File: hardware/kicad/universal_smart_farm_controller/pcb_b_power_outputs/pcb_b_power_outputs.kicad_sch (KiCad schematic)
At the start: 55 parts, among them J1 Conn_01x12, J10 Conn_01x02, J11 Conn_01x02, J12 Conn_01x02, J13 Conn_01x02, J14 Conn_01x02, J15 Conn_01x02, J16 Conn_01x02, J17 Conn_01x02, J18 Conn_01x02, Q1 AO3400A, Q2 AO3400A, Q3 AO3400A, Q4 AO3400A, Q5 AO3400A, Q6 AO3400A, Q7 AO3400A, Q8 AO3400A

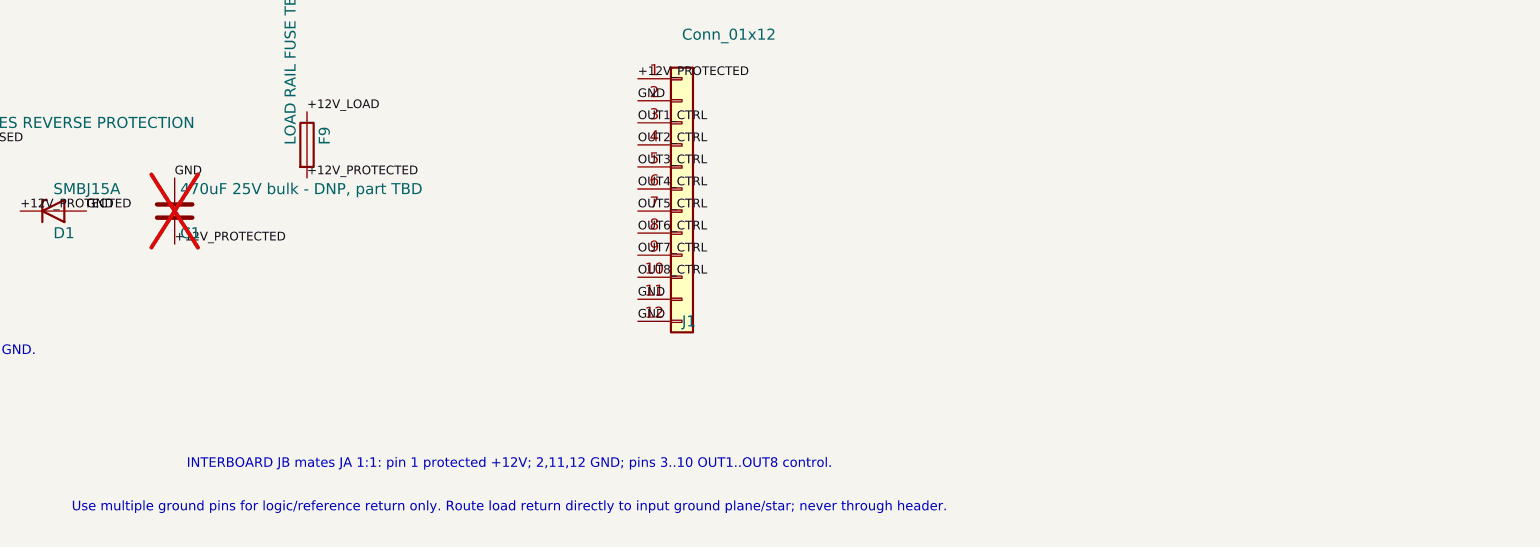
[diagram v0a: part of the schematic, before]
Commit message: Add PCB-B power LED, document PCB-A GPIO2 status LED, fix ADS1X15 lib_deps name
Co-authored-by: tomnyle <175001228+tomnyle@users.noreply.github.com>
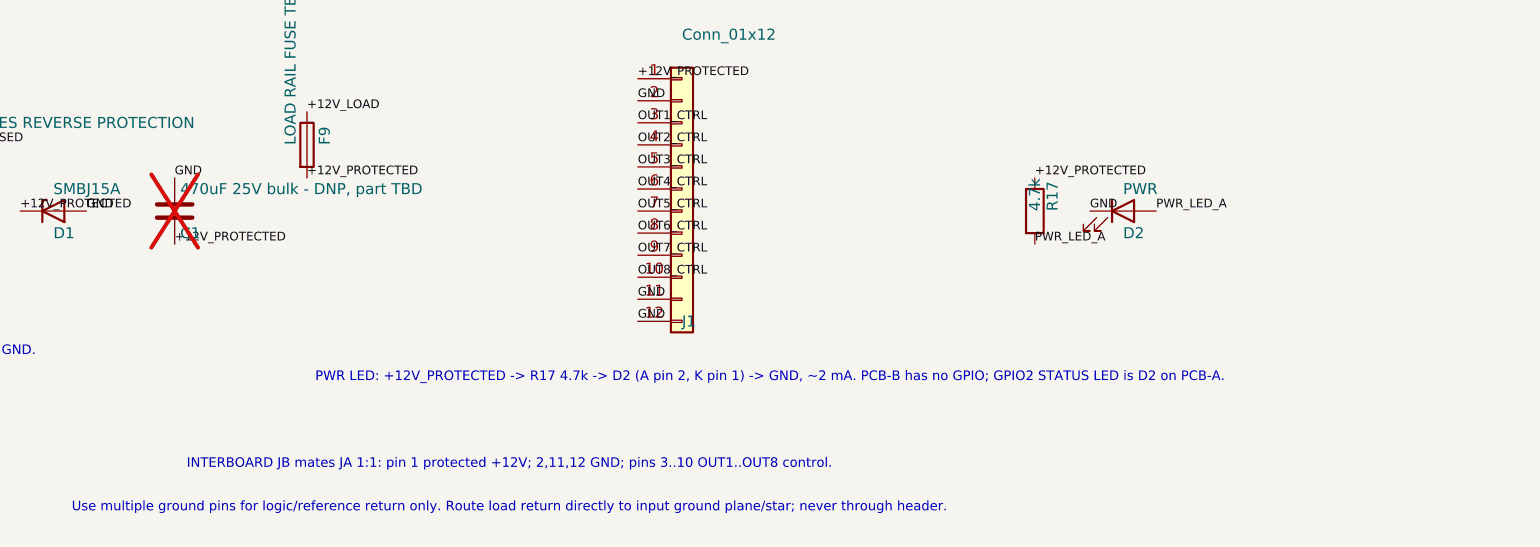
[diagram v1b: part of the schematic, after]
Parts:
- added D2: PWR, LED_SMD:LED_0805_2012Metric, symbol Device:LED
- added R17: 4.7k, Resistor_SMD:R_0805_2012Metric, symbol Device:R
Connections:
- net +12V_PROTECTED: now also R17.1
- net GND: now also D2.1 (K)
- new net PWR_LED_A: D2.2 (A), R17.2
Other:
- note added: "PWR LED: +12V_PROTECTED -> R17 4.7k -> D2 (A pin 2, K pin 1) -> GND, ~2 mA. PCB-B has no GPIO; GPIO2 STATUS LED is D2 on PCB-A."
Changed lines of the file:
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@@
+		)
+	)
+	(symbol
+		(lib_id "Device:R")
+		(at 190.5 50.8 0)
+		(unit 1)
+		(exclude_from_sim no)
+		(in_bom yes)
+		(on_board yes)
+		(dnp no)
+		(fields_autoplaced no)
+		(property "Reference" "R17"
+			(at 192.532 50.8 90)
+			(effects
+				(font
+					(size 1.27 1.27)
+				)
+				(justify left)
+			)
+		)
+		(property "Value" "4.7k"
+			(at 190.5 50.8 90)
+			(effects
+				(font
+					(size 1.27 1.27)
+				)
+				(justify left)
+			)
+		)
+		(property "Footprint" "Resistor_SMD:R_0805_2012Metric"
+			(at 188.722 50.8 90)
+			(effects
+				(font
+					(size 1.27 1.27)
+				)
+				(hide yes)
+			)
+		)
+		(pin "1"
+		)
+		(pin "2"
+		)
+		(instances
+			(project "PCB-B 12V Power and Outputs Rev A reference"
+				(path "/99b31c03-3e14-461b-a0bf-97759b6823f3"
+					(reference "R17")
+					(unit 1)
+				)
+			)
+		)
+	)
+	(symbol
+		(lib_id "Device:LED")
+		(at 200.66 50.8 0)
+		(unit 1)
+		(exclude_from_sim no)
+		(in_bom yes)
+		(on_board yes)
+		(dnp no)
+		(fields_autoplaced no)
+		(property "Reference" "D2"
+			(at 200.66 53.34 0)
+			(effects
+				(font
+					(size 1.27 1.27)
+				)
+				(justify left)
+			)
+		)
+		(property "Value" "PWR"
+			(at 200.66 48.26 0)
+			(effects
+				(font
+					(size 1.27 1.27)
+				)
+				(justify left)
+			)
+		)
+		(property "Footprint" "LED_SMD:LED_0805_2012Metric"
+			(at 200.66 50.8 0)
+			(effects
+				(font
+					(size 1.27 1.27)
+				)
+				(hide yes)
+			)
+		)
+		(pin "1"
+		)
+		(pin "2"
+		)
+		(instances
+			(project "PCB-B 12V Power and Outputs Rev A reference"
+				(path "/99b31c03-3e14-461b-a0bf-97759b6823f3"
+					(reference "D2")
+					(unit 1)
+				)
+			)
 		)
 	)
@@
 		)
 	)
+	(label "+12V_PROTECTED"
+		(at 190.5 46.99 0)
+		(effects
+			(font
+				(size 1 1)
+			)
+			(justify left bottom)
+		)
+	)
+	(label "PWR_LED_A"
+		(at 190.5 54.61 0)
+		(effects
+			(font
+				(size 1 1)
+			)
+			(justify left bottom)
+		)
+	)
+	(label "GND"
+		(at 196.85 50.8 0)
+		(effects
+			(font
+				(size 1 1)
+			)
+			(justify left bottom)
+		)
+	)
+	(label "PWR_LED_A"
+		(at 204.47 50.8 0)
+		(effects
+			(font
+				(size 1 1)
+			)
+			(justify left bottom)
+		)
+	)
+	(text "PWR LED: +12V_PROTECTED -> R17 4.7k -> D2 (A pin 2, K pin 1) -> GND, ~2 mA. PCB-B has no GPIO; GPIO2 STATUS LED is D2 on PCB-A."
+		(exclude_from_sim no)
+		(at 160 70 0.0000)
+		(effects
+			(font
+				(size 1.1 1.1)
+			)
+		)
+	)
